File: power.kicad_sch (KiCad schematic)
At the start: 29 parts, among them J1 USB_C_Receptacle_USB2.0_14P, SW5 SW_Push, U2 nPM1300-QEXX, U8 TPD3E001DRLR

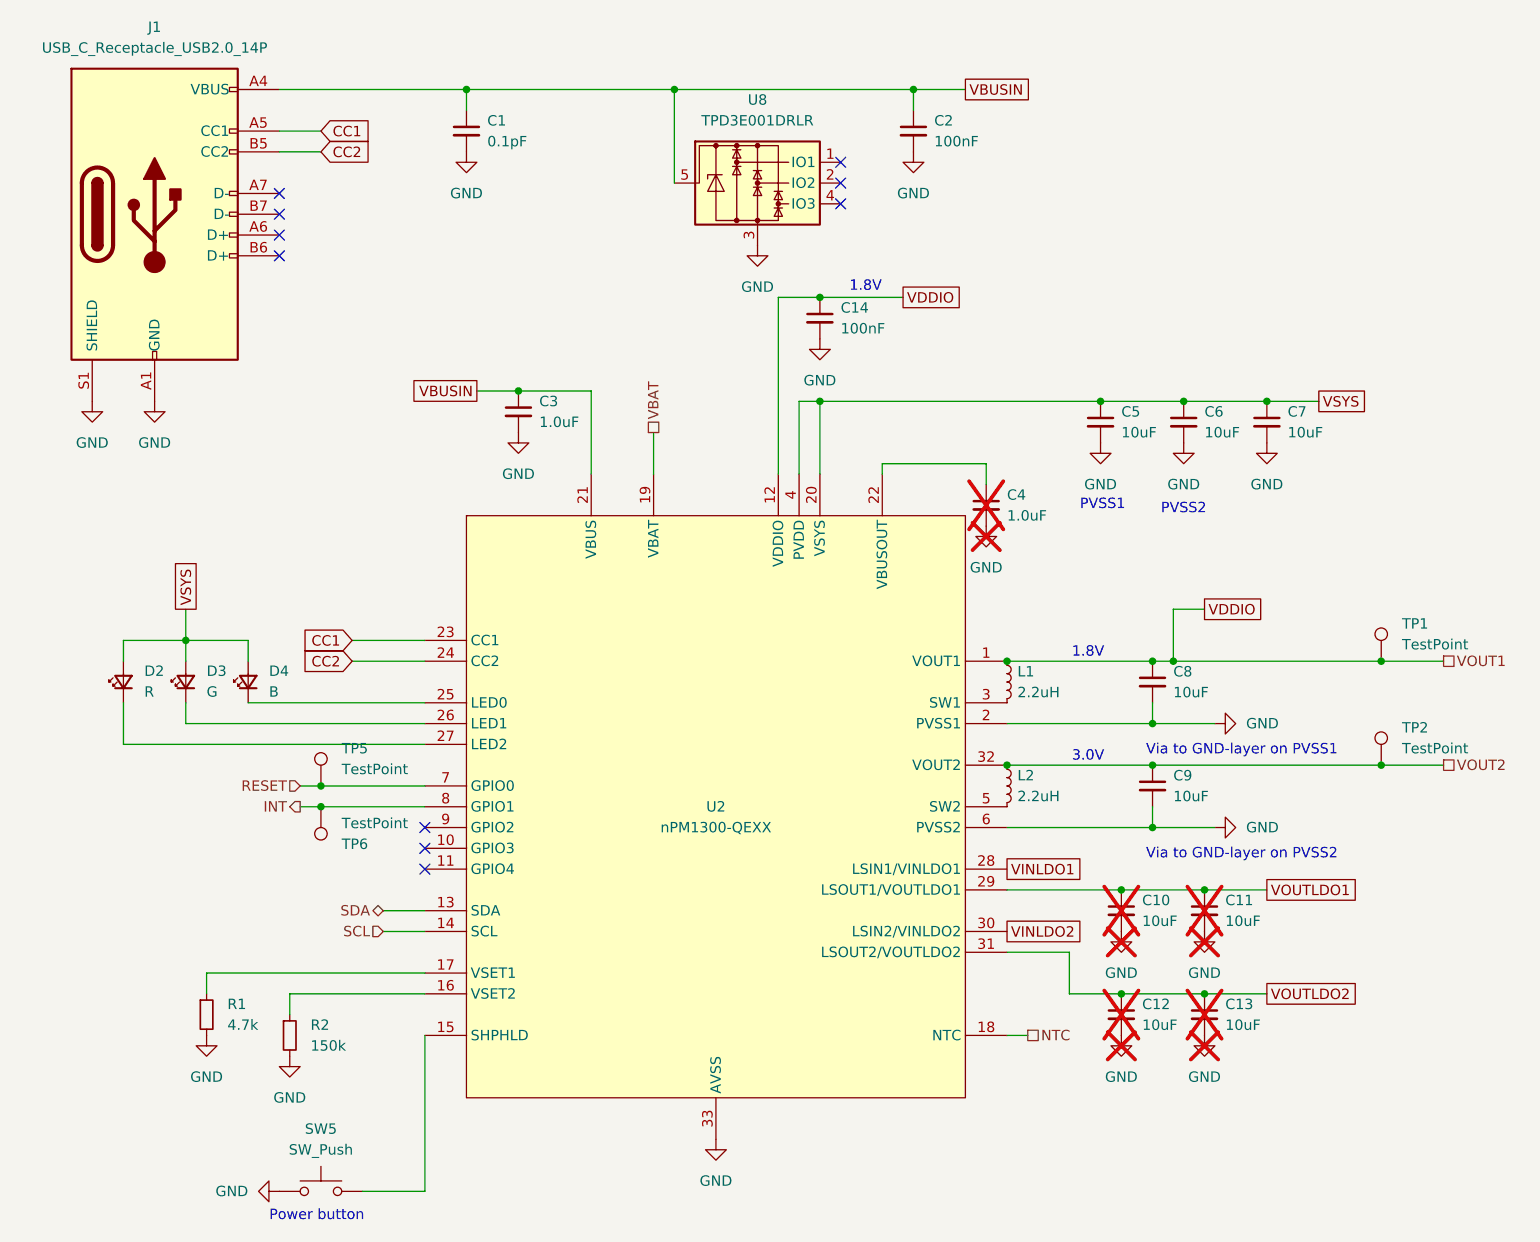
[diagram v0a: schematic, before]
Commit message: route PMIC
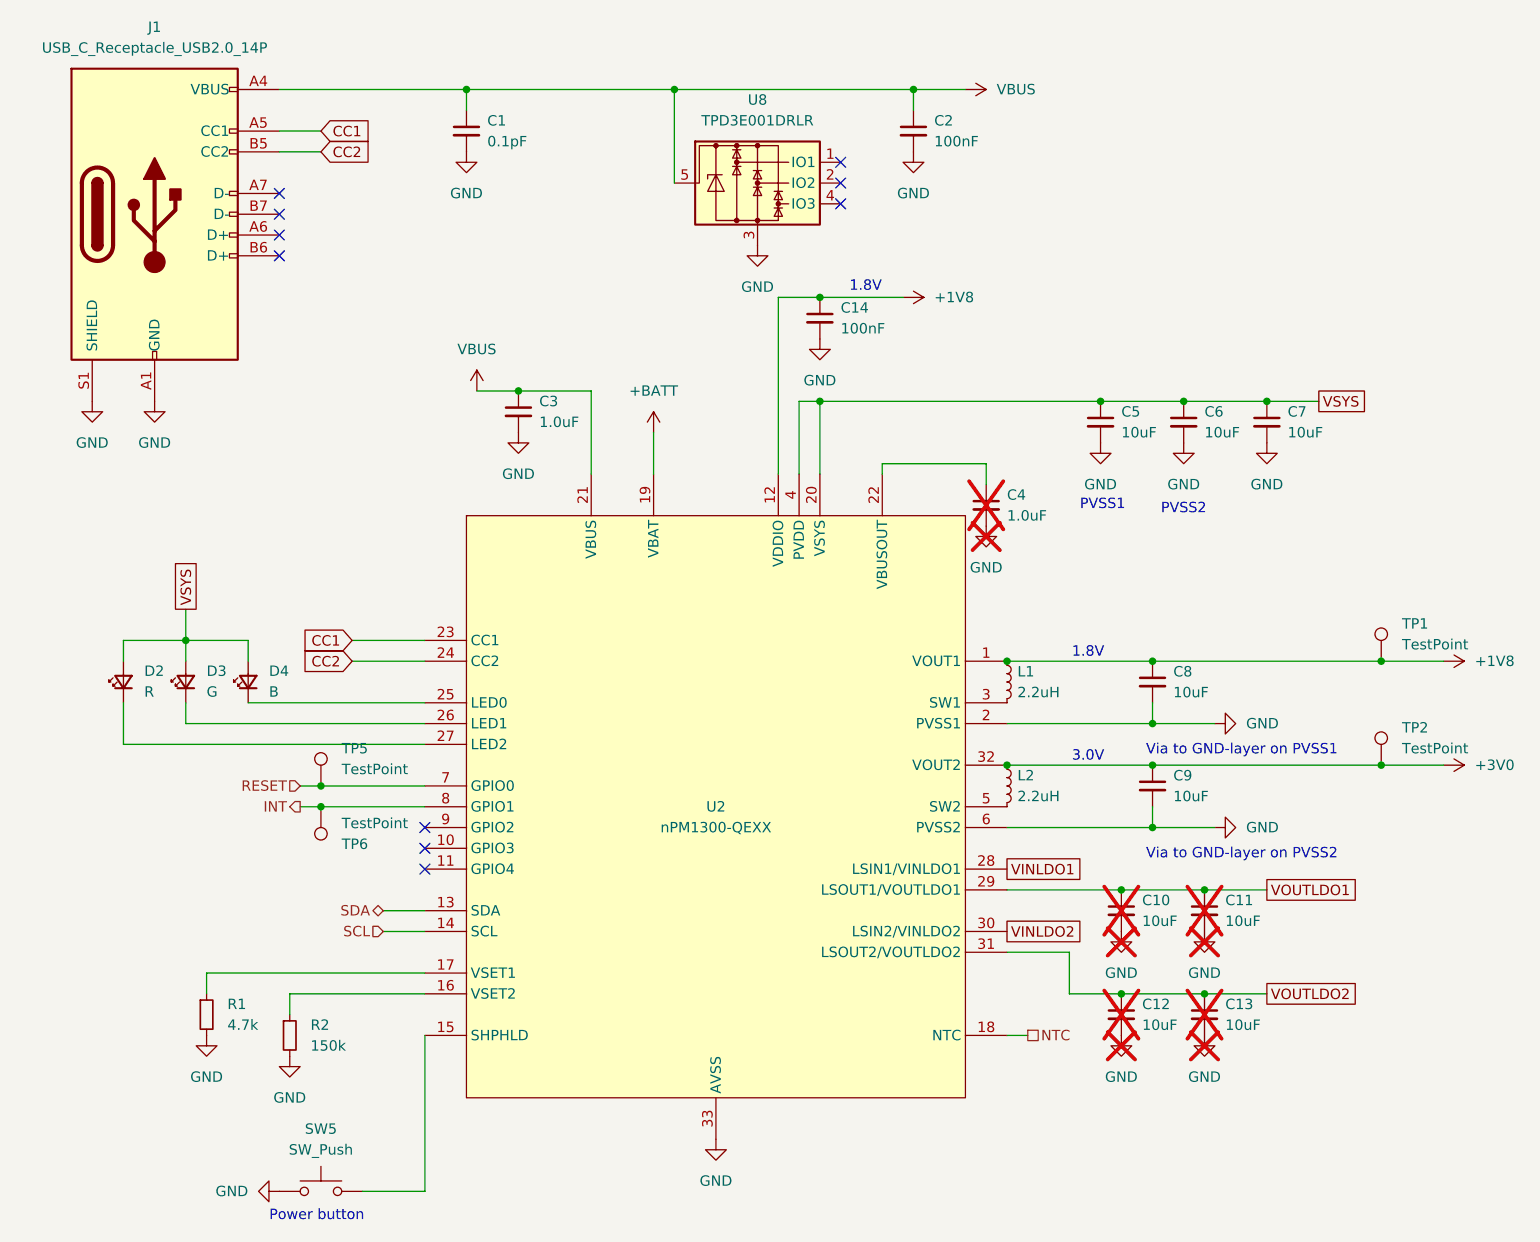
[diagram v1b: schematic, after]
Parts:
- TP1, TP2, TP5, TP6: footprint (none) -> TestPoint:TestPoint_Pad_1.0x1.0mm
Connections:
- net VBAT renamed +BATT
- net VBUSIN renamed VBUS
- net VDDIO renamed +1V8
- net VOUT2 renamed +3V0

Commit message: power button
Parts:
- SW5: footprint (none) -> Button_Switch_SMD:SW_SPST_PTS647_Sx50
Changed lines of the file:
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@@
 			)
 		)
-		(property "Footprint" ""
+		(property "Footprint" "Button_Switch_SMD:SW_SPST_PTS647_Sx50"
 			(at 67.31 163.83 0)
 			(effects
